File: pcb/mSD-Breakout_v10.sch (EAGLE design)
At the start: 17 parts, among them IC1 74LVC244APW, IC2 LDO-TS5204, X1 PASSER, X2 PASSER, X3 PASSER

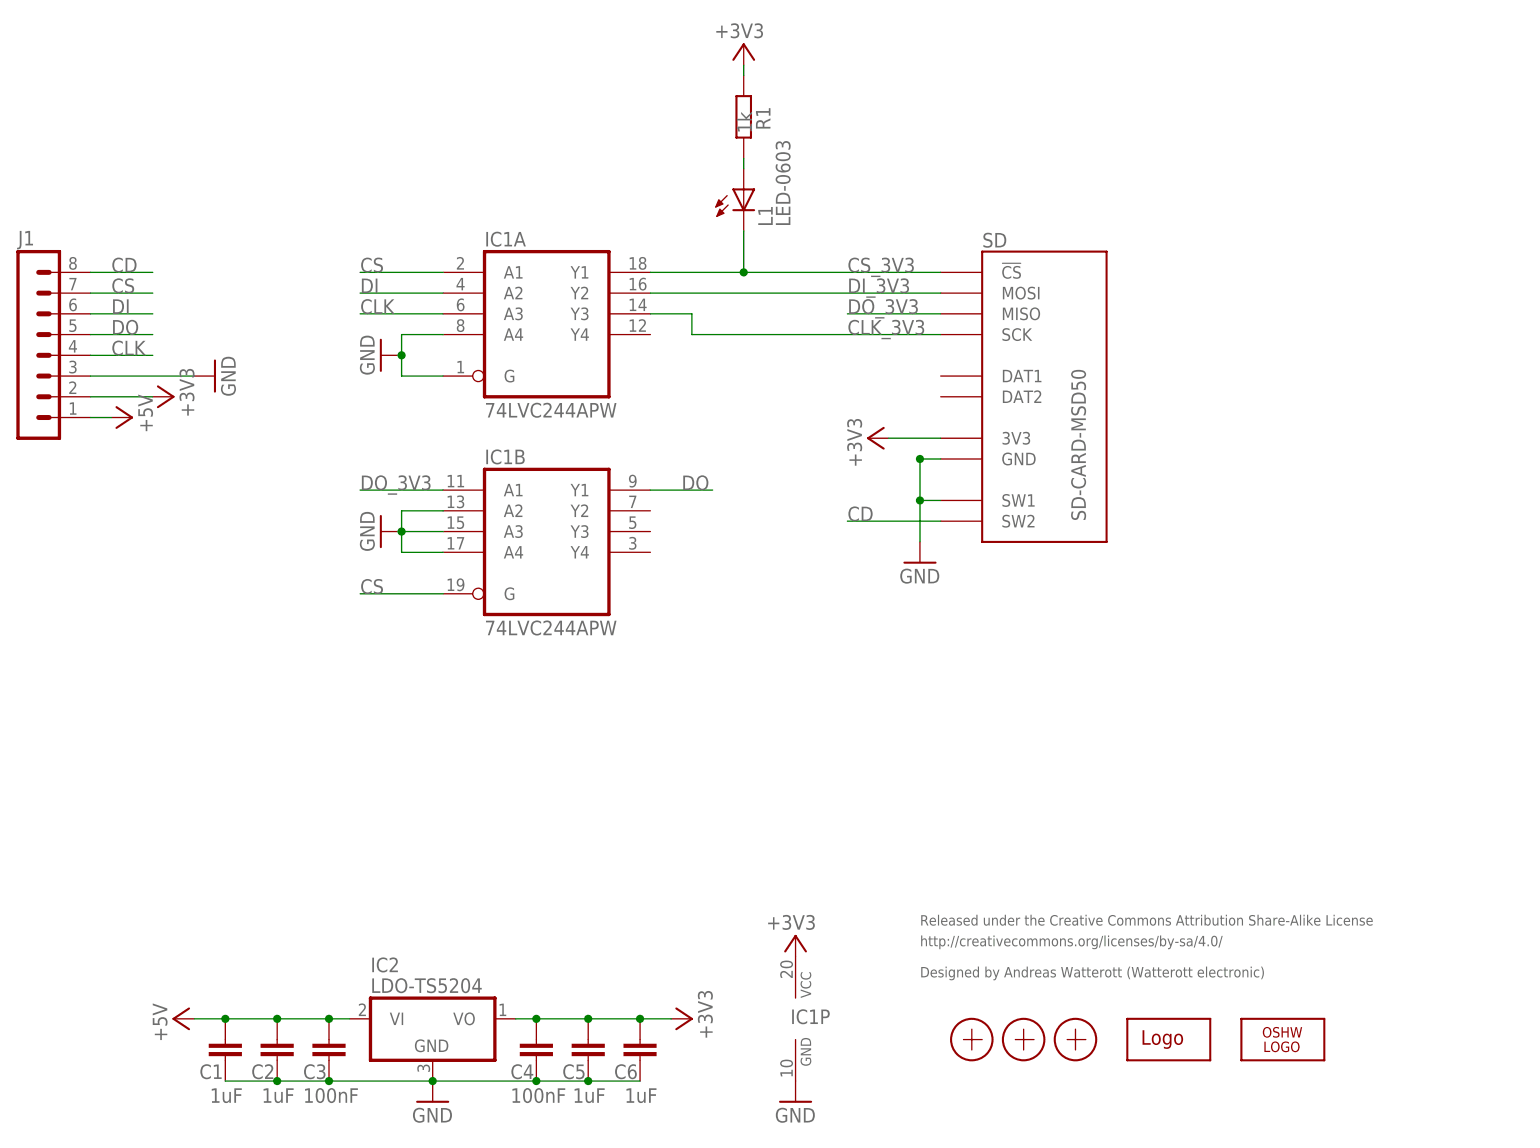
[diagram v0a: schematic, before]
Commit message: updated schematics
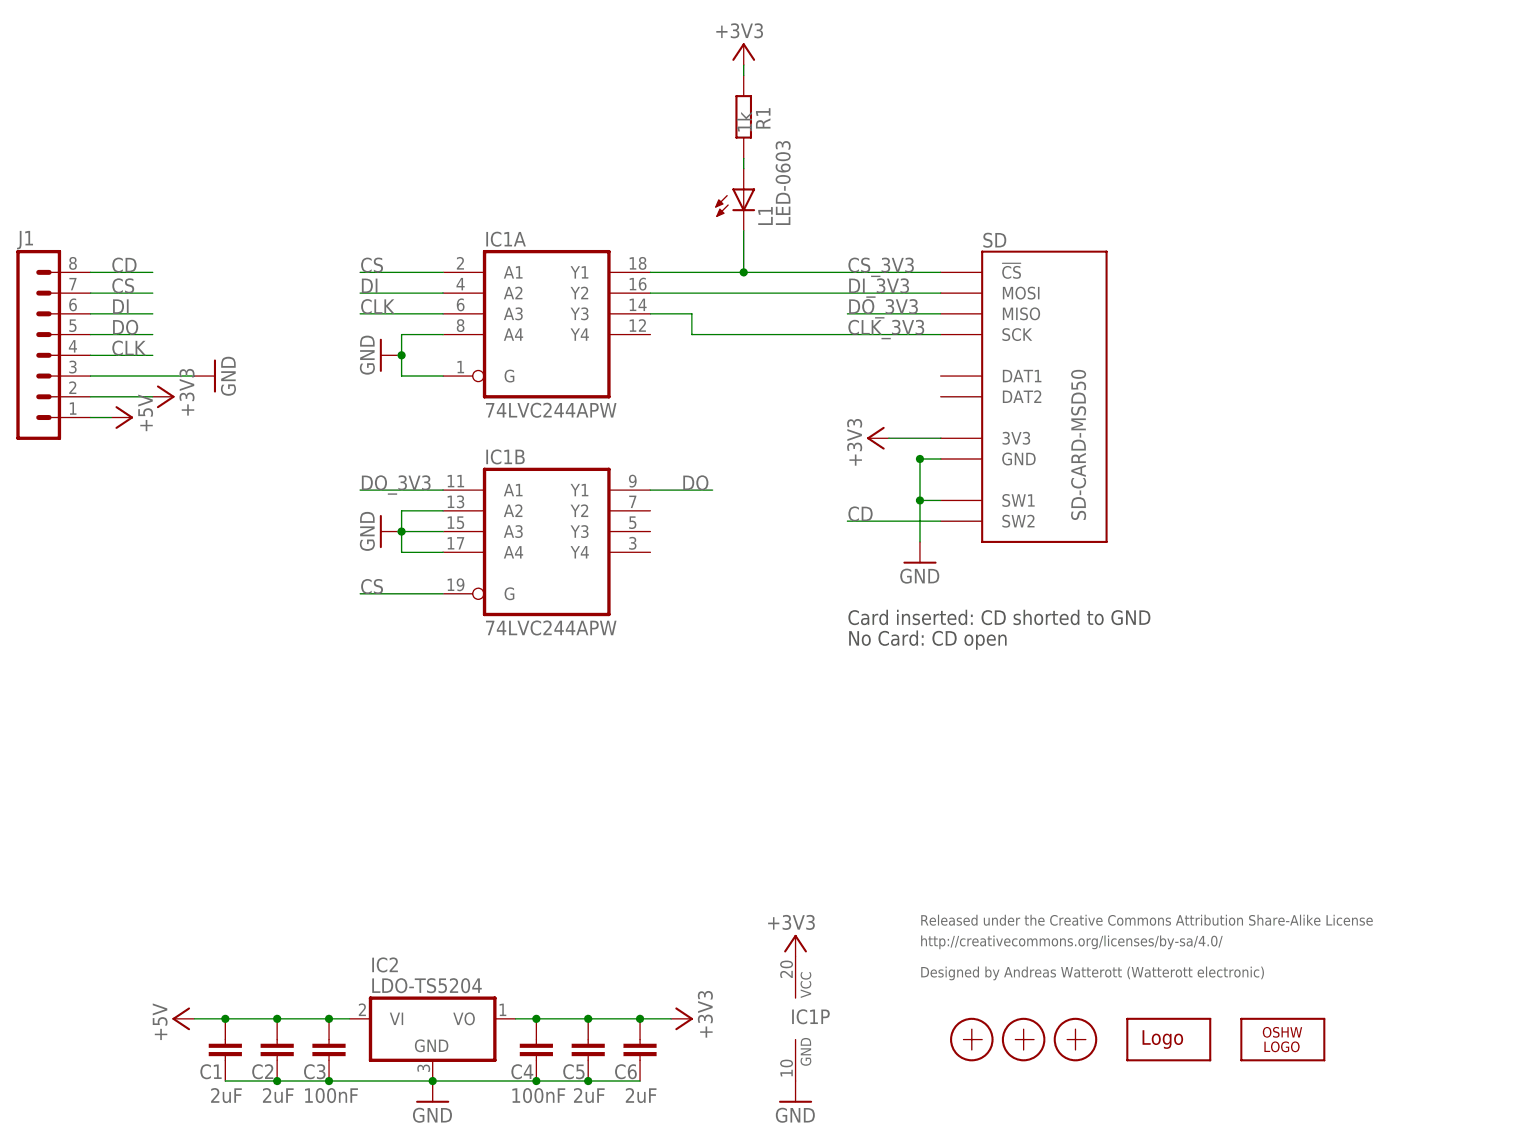
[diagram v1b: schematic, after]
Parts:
- C1, C2, C5, C6: value 1uF -> 2uF
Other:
- note added: "Card inserted: CD shorted to GND"
- note added: "No Card: CD open"
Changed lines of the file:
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@@
 <setting verticaltext="up"/>
 </settings>
-<grid distance="0.05" unitdist="inch" unit="inch" style="lines" multiple="1" display="yes" altdistance="0.025" altunitdist="inch" altunit="inch"/>
+<grid distance="0.1" unitdist="inch" unit="inch" style="lines" multiple="1" display="no" altdistance="0.01" altunitdist="inch" altunit="inch"/>
 <layers>
 <layer number="1" name="Top" color="4" fill="1" visible="no" active="no"/>
@@
 <part name="C3" library="rcl" deviceset="C-EU" device="C0603" value="100nF"/>
 <part name="C4" library="rcl" deviceset="C-EU" device="C0603" value="100nF"/>
-<part name="C2" library="rcl" deviceset="C-EU" device="C0603" value="1uF"/>
+<part name="C2" library="rcl" deviceset="C-EU" device="C0603" value="2uF"/>
 <part name="FRAME1" library="frames" deviceset="A4L-LOC" device=""/>
 <part name="+3V4" library="supply1" deviceset="+3V3" device=""/>
-<part name="C5" library="rcl" deviceset="C-EU" device="C0603" value="1uF"/>
+<part name="C5" library="rcl" deviceset="C-EU" device="C0603" value="2uF"/>
 <part name="P+3" library="supply1" deviceset="+5V" device=""/>
 <part name="SD" library="we-con" deviceset="SD-CARD" device="-MSD50"/>
@@
 <part name="LOGO2" library="we-symbol" deviceset="LOGO" device="-SPARK_PLACE"/>
 <part name="R1" library="rcl" deviceset="R-EU_" device="R0603" value="1k"/>
-<part name="C6" library="rcl" deviceset="C-EU" device="C0603" value="1uF"/>
-<part name="C1" library="rcl" deviceset="C-EU" device="C0603" value="1uF"/>
+<part name="C6" library="rcl" deviceset="C-EU" device="C0603" value="2uF"/>
+<part name="C1" library="rcl" deviceset="C-EU" device="C0603" value="2uF"/>
 <part name="L1" library="we-opto" deviceset="LED" device="-0603"/>
 <part name="+3V1" library="supply1" deviceset="+3V3" device=""/>
@@
 <text x="161.29" y="29.21" size="1.27" layer="95">http://creativecommons.org/licenses/by-sa/4.0/</text>
 <text x="161.29" y="25.4" size="1.27" layer="95">Designed by Andreas Watterott (Watterott electronic)</text>
+<text x="152.4" y="68.58" size="1.778" layer="97">Card inserted: CD shorted to GND</text>
+<text x="152.4" y="66.04" size="1.778" layer="97">No Card: CD open</text>
 </plain>
 <instances>

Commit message: updated schematic and layout files
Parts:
- IC2: value LDO-TS5204 -> LDO-TS5204-3V3
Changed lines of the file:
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@@
 <?xml version="1.0" encoding="utf-8"?>
 <!DOCTYPE eagle SYSTEM "eagle.dtd">
-<eagle version="6.5.0">
+<eagle version="6.6.0">
 <drawing>
 <settings>
@@
 <part name="P+3" library="supply1" deviceset="+5V" device=""/>
 <part name="SD" library="we-con" deviceset="SD-CARD" device="-MSD50"/>
-<part name="IC2" library="we-power" deviceset="LDO" device="-TS5204"/>
+<part name="IC2" library="we-power" deviceset="LDO" device="-TS5204" value="LDO-TS5204-3V3"/>
 <part name="IC1" library="we-chip" deviceset="74*244" device="PW" technology="LVC" value="74LVC244APW"/>
 <part name="J1" library="we-con" deviceset="MA08-1" device=""/>
